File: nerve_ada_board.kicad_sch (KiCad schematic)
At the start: 58 parts, among them J1 TC2050-IDC, J10 WS2812B, J3 2171750001, J4 Camera, J5 CAN1, J6 CAN2, J7 PA4-7, J8 PB4-5, J9 PC1-3, SW1 SPST, SW2 SPST, SW3 SPDT, SW4 SPST, U1 LD1117S33TR_SOT223, U10 TXB0102DCT, U2 STM32F446RET, U5 XBP9B-DMWT-002, U6 32k768, U7 SAM-M10Q, Y1 8M

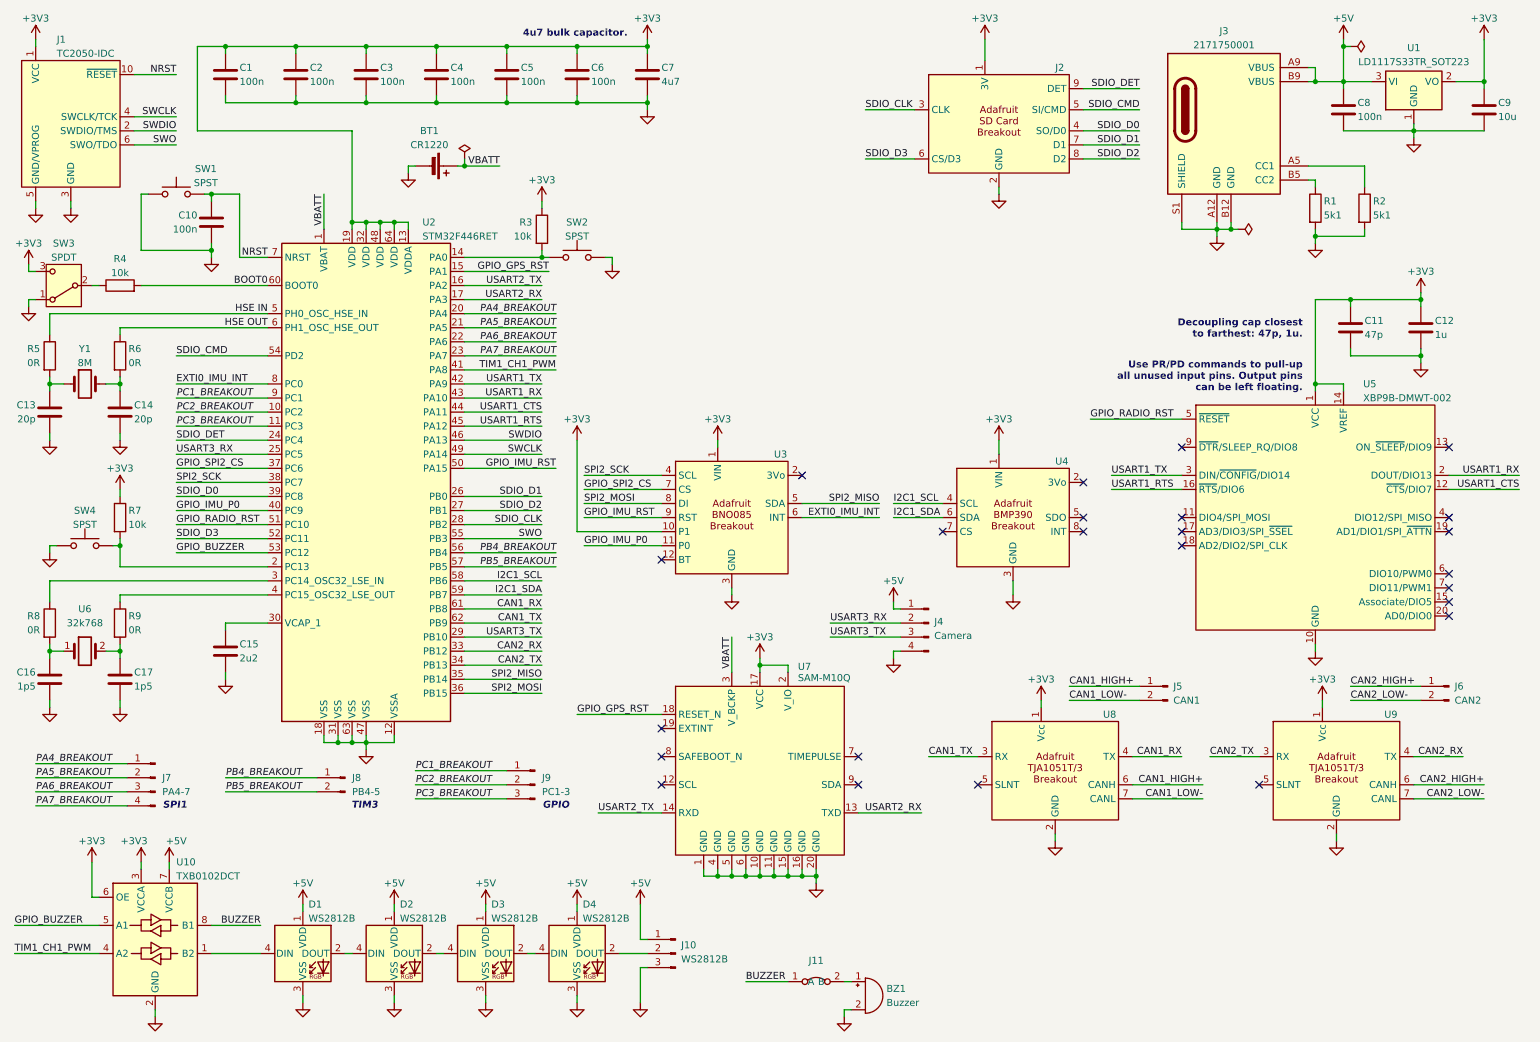
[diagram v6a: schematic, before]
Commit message: Switch to hierarchical labels and major clean up
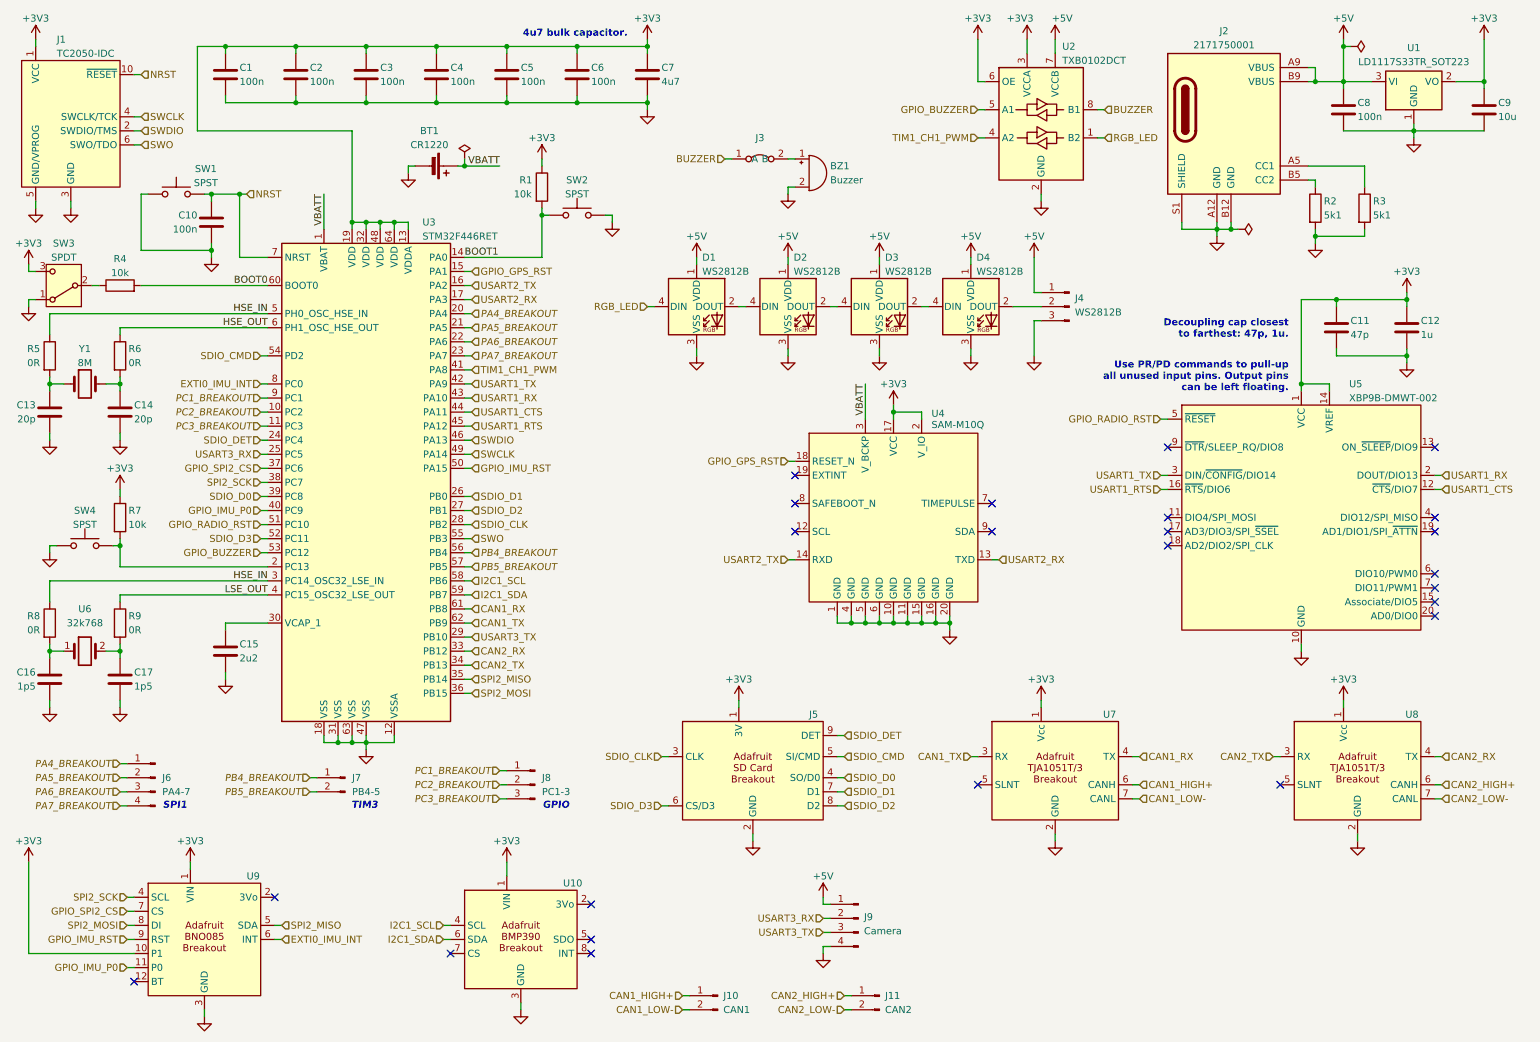
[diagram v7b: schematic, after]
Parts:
- renumbered J5 to J10, J6 to J11, J3 to J2, J11 to J3, J10 to J4, J2 to J5, J7 to J6, J8 to J7, J9 to J8, J4 to J9, R3 to R1, R1 to R2, R2 to R3, U4 to U10, U10 to U2, U2 to U3, U7 to U4, U8 to U7, U9 to U8, U3 to U9
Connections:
- net HSE IN is gone; now on net HSE_IN: R5.1, U3.5 (PH0_OSC_HSE_IN)
- net BOOT1: now reaches R1.2, SW2.1, U3.14 (PA0)
- net RGB_LED: now reaches D1.4 (DIN), U2.1 (B2)
- net LSE_OUT: now reaches R9.1, U3.4 (PC15_OSC32_LSE_OUT)
- net HSE_IN: now reaches R8.1, U3.3 (PC14_OSC32_LSE_IN)
- net HSE OUT renamed HSE_OUT
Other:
- moved on the sheet: BZ1, C11, C12, D1, D2, D3, D4, J10, J11, J3, J4, J5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

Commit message: Update library and fix annotations
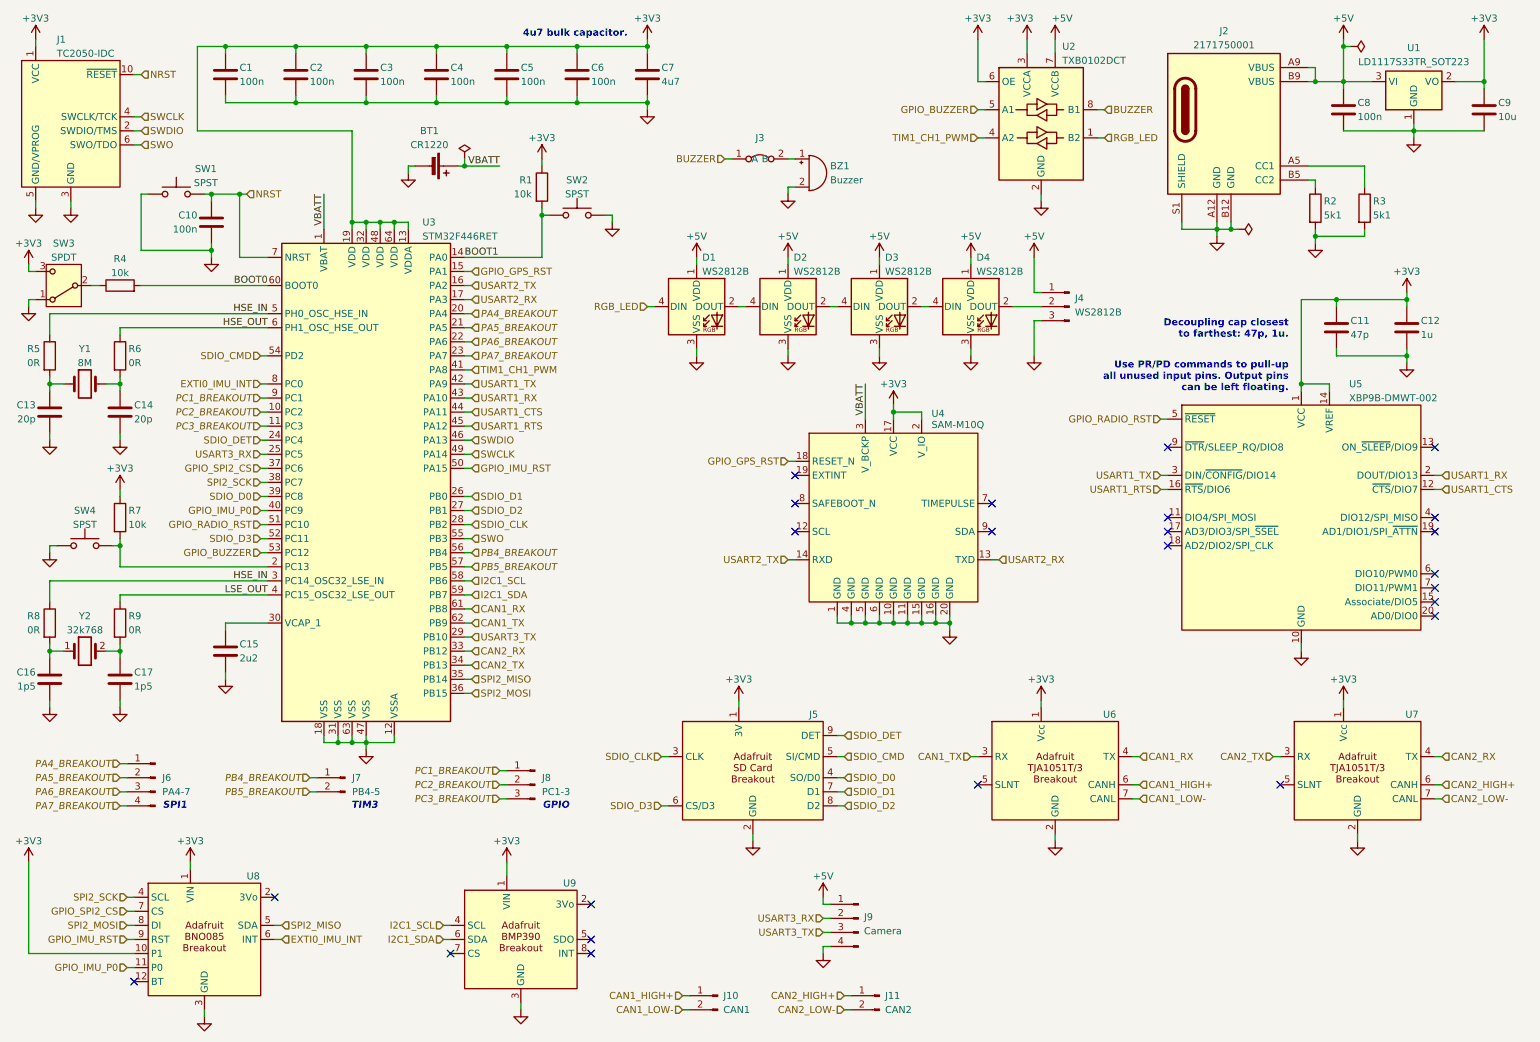
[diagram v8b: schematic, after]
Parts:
- removed U6: 32k768, common:xtal_abs25-32.768khz-6-t, symbol common:abs25-32.768khz-6-t
- added Y2: 32k768, common:xtal_abs25-32.768khz-6-t, symbol common:abs25-32.768khz-6-t
- renumbered U7 to U6, U8 to U7, U9 to U8, U10 to U9
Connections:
- net at C16.1, R8.2: now also Y2.1
- net at C17.1, R9.2: now also Y2.2
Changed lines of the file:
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@@
 		(on_board yes)
 		(dnp no)
-		(property "Reference" "U10"
+		(property "Reference" "U9"
 			(at 111.76 170.18 0)
 			(effects
@@
 			(project "nerve_ada_board"
 				(path "/c0277862-b3f2-4e0e-986f-34702f0543f0"
-					(reference "U10")
+					(reference "U9")
 					(unit 1)
 				)
@@
 	)
 	(symbol
-		(lib_id "common:abs25-32.768khz-6-t")
-		(at 25.4 128.27 0)
-		(unit 1)
-		(exclude_from_sim no)
-		(in_bom yes)
-		(on_board yes)
-		(dnp no)
-		(fields_autoplaced yes)
-		(property "Reference" "U6"
-			(at 25.4 120.65 0)
-			(effects
-				(font
-					(size 1.27 1.27)
-				)
-			)
-		)
-		(property "Value" "32k768"
-			(at 25.4 123.19 0)
-			(effects
-				(font
-					(size 1.27 1.27)
-				)
-			)
-		)
-		(property "Footprint" "common:xtal_abs25-32.768khz-6-t"
-			(at 25.4 128.27 0)
-			(effects
-				(font
-					(size 1.27 1.27)
-				)
-				(hide yes)
-			)
-		)
-		(property "Datasheet" "https://abracon.com/Resonators/abs25.pdf"
-			(at 25.4 128.27 0)
-			(effects
-				(font
-					(size 1.27 1.27)
-				)
-				(hide yes)
-			)
-		)
-		(property "Description" "CRYSTAL 32.7680KHz 6PF SMD"
-			(at 25.4 128.27 0)
-			(effects
-				(font
-					(size 1.27 1.27)
-				)
-				(hide yes)
-			)
-		)
-		(property "Manufacturer" "Abracon LLC"
-			(at 25.4 128.27 0)
-			(effects
-				(font
-					(size 1.27 1.27)
-				)
-				(hide yes)
-			)
-		)
-		(property "Manufacturer Part Number" "ABS25-32.768KHZ-6-T"
-			(at 25.4 128.27 0)
-			(effects
-				(font
-					(size 1.27 1.27)
-				)
-				(hide yes)
-			)
-		)
-		(property "Distributor" "DigiKey"
-			(at 25.4 128.27 0)
-			(effects
-				(font
-					(size 1.27 1.27)
-				)
-				(hide yes)
-			)
-		)
-		(property "Distributor Part Number" "535-10240-1-ND"
-			(at 25.4 128.27 0)
-			(effects
-				(font
-					(size 1.27 1.27)
-				)
-				(hide yes)
-			)
-		)
-		(property "Distributor Link" "https://www.digikey.ca/en/products/detail/abracon-llc/ABS25-32-768KHZ-6-T/2217986"
-			(at 25.4 128.27 0)
-			(effects
-				(font
-					(size 1.27 1.27)
-				)
-				(hide yes)
-			)
-		)
-		(pin "2"
-		)
-		(pin "1"
-		)
-		(instances
-			(project ""
-				(path "/c0277862-b3f2-4e0e-986f-34702f0543f0"
-					(reference "U6")
-					(unit 1)
-				)
-			)
-		)
-	)
-	(symbol
 		(lib_id "Device:C")
 		(at 31.75 85.09 0)
@@
 		(on_board yes)
 		(dnp no)
-		(property "Reference" "U7"
+		(property "Reference" "U6"
 			(at 209.296 139.7 0)
 			(effects
@@
 			(project "nerve_ada_board"
 				(path "/c0277862-b3f2-4e0e-986f-34702f0543f0"
-					(reference "U7")
+					(reference "U6")
 					(unit 1)
 				)
@@
 		(on_board yes)
 		(dnp no)
-		(property "Reference" "U8"
+		(property "Reference" "U7"
 			(at 263.906 139.7 0)
 			(effects
@@
 			(project "nerve_ada_board"
 				(path "/c0277862-b3f2-4e0e-986f-34702f0543f0"
-					(reference "U8")
+					(reference "U7")
 					(unit 1)
 				)
@@
 	)
 	(symbol
+		(lib_id "common:abs25-32.768khz-6-t")
+		(at 25.4 128.27 0)
+		(unit 1)
+		(exclude_from_sim no)
+		(in_bom yes)
+		(on_board yes)
+		(dnp no)
+		(property "Reference" "Y2"
+			(at 25.4 121.92 0)
+			(effects
+				(font
+					(size 1.27 1.27)
+				)
+			)
+		)
+		(property "Value" "32k768"
+			(at 25.4 124.46 0)
+			(effects
+				(font
+					(size 1.27 1.27)
+				)
+			)
+		)
+		(property "Footprint" "common:xtal_abs25-32.768khz-6-t"
+			(at 25.4 128.27 0)
+			(effects
+				(font
+					(size 1.27 1.27)
+				)
+				(hide yes)
+			)
+		)
+		(property "Datasheet" "https://abracon.com/Resonators/abs25.pdf"
+			(at 25.4 128.27 0)
+			(effects
+				(font
+					(size 1.27 1.27)
+				)
+				(hide yes)
+			)
+		)
+		(property "Description" "CRYSTAL 32.7680KHz 6PF SMD"
+			(at 25.4 128.27 0)
+			(effects
+				(font
+					(size 1.27 1.27)
+				)
+				(hide yes)
+			)
+		)
+		(property "Manufacturer" "Abracon LLC"
+			(at 25.4 128.27 0)
+			(effects
+				(font
+					(size 1.27 1.27)
+				)
+				(hide yes)
+			)
+		)
+		(property "Manufacturer Part Number" "ABS25-32.768KHZ-6-T"
+			(at 25.4 128.27 0)
+			(effects
+				(font
+					(size 1.27 1.27)
+				)
+				(hide yes)
+			)
+		)
+		(property "Distributor" "DigiKey"
+			(at 25.4 128.27 0)
+			(effects
+				(font
+					(size 1.27 1.27)
+				)
+				(hide yes)
+			)
+		)
+		(property "Distributor Part Number" "535-10240-1-ND"
+			(at 25.4 128.27 0)
+			(effects
+				(font
+					(size 1.27 1.27)
+				)
+				(hide yes)
+			)
+		)
+		(property "Distributor Link" "https://www.digikey.ca/en/products/detail/abracon-llc/ABS25-32-768KHZ-6-T/2217986"
+			(at 25.4 128.27 0)
+			(effects
+				(font
+					(size 1.27 1.27)
+				)
+				(hide yes)
+			)
+		)
+		(pin "2"
+		)
+		(pin "1"
+		)
+		(instances
+			(project ""
+				(path "/c0277862-b3f2-4e0e-986f-34702f0543f0"
+					(reference "Y2")
+					(unit 1)
+				)
+			)
+		)
+	)
+	(symbol
 		(lib_id "power:+3V3")
 		(at 15.24 166.37 0)
@@
 		(on_board yes)
 		(dnp no)
-		(property "Reference" "U9"
+		(property "Reference" "U8"
 			(at 54.61 168.91 0)
 			(effects
@@
 			(project "nerve_ada_board"
 				(path "/c0277862-b3f2-4e0e-986f-34702f0543f0"
-					(reference "U9")
+					(reference "U8")
 					(unit 1)
 				)
